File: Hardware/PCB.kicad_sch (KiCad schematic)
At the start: 9 parts, among them J1 Conn_01x04_Pin, U1 ME54BS01_V1.0, U2 MCP1700x-330xxTO

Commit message: Work on PCB
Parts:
- J1: footprint (none) -> Connector_PinHeader_2.54mm:PinHeader_1x04_P2.54mm_Vertical
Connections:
- net +3.3V: no longer S1.3
- net GND: no longer U1.1 (GND)
- net dividerPower1: now also U1.3 (P1.10)
- net dividerPower2: now also U1.4 (P1.11/AIN4)
- net reset: now also U1.24 (P0.01)
- no-connect marks 21 -> 23
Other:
- note added: "Was using battery connector footpring Connector_JST:JST_PH_S2B-PH-K_1x02_P2.00mm_Horizontal"
- moved on the sheet: BATT1, J1, Probe1, Probe2, R1, R2, S1, U1, U2

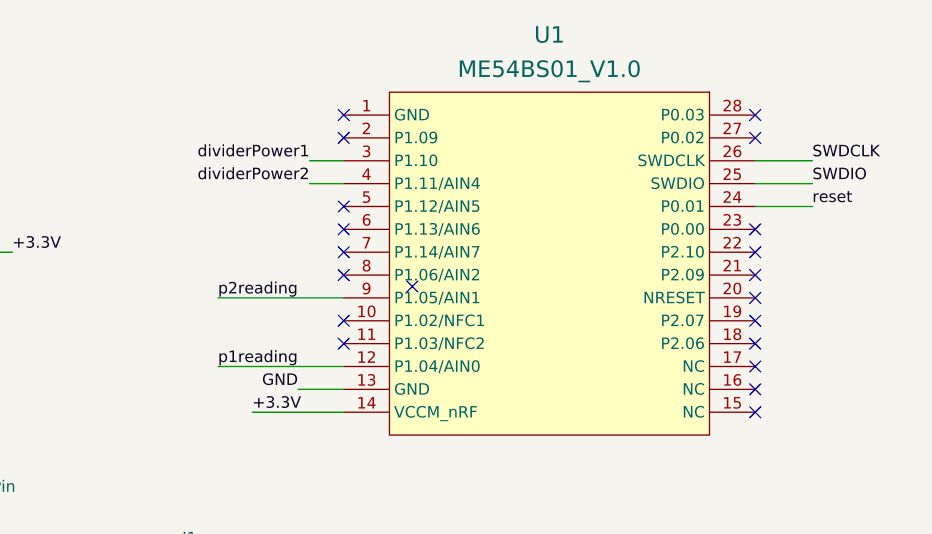
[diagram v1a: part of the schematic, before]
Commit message: Update PCB with new pin outs
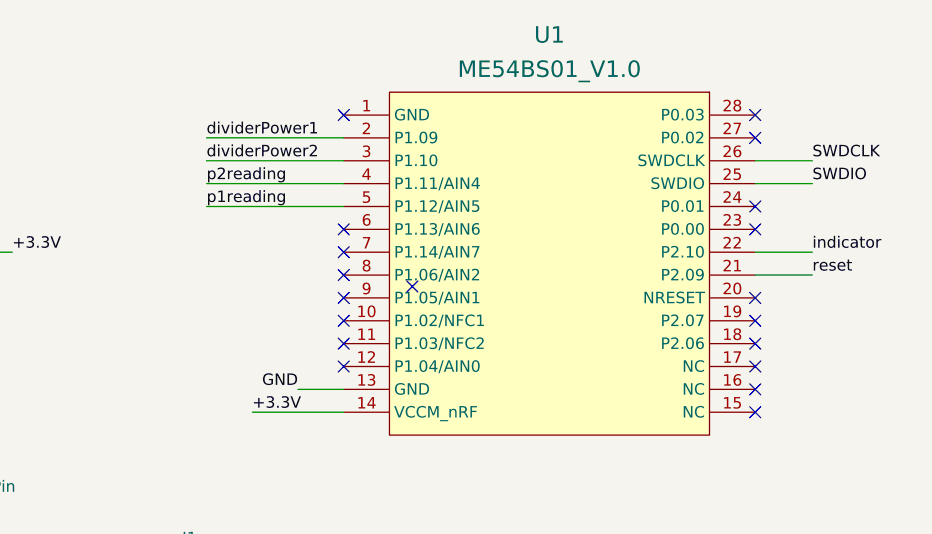
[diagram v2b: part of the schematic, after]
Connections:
- net dividerPower1: now also U1.2 (P1.09); no longer U1.3 (P1.10)
- net dividerPower2: now also U1.3 (P1.10); no longer U1.4 (P1.11/AIN4)
- net p1reading: now also U1.5 (P1.12/AIN5); no longer U1.12 (P1.04/AIN0)
- net p2reading: now also U1.4 (P1.11/AIN4); no longer U1.9 (P1.05/AIN1)
- net reset: now also U1.21 (P2.09); no longer U1.24 (P0.01)
- net indicator: now reaches U1.22 (P2.10)
- no-connect marks 23 -> 22
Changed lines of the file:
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@@
 	)
 	(no_connect
-		(at 154.94 38.1)
+		(at 200.66 38.1)
 	)
 	(no_connect
@@
 	)
 	(no_connect
+		(at 154.94 48.26)
+	)
+	(no_connect
+		(at 154.94 40.64)
+	)
+	(no_connect
 		(at 200.66 30.48)
 	)
@@
 	)
 	(no_connect
-		(at 200.66 43.18)
+		(at 200.66 60.96)
+	)
+	(no_connect
+		(at 33.02 45.72)
+	)
+	(no_connect
+		(at 200.66 50.8)
 	)
 	(no_connect
@@
 	)
 	(no_connect
-		(at 200.66 60.96)
-	)
-	(no_connect
-		(at 154.94 30.48)
-	)
-	(no_connect
-		(at 33.02 45.72)
-	)
-	(no_connect
-		(at 200.66 50.8)
-	)
-	(no_connect
-		(at 200.66 45.72)
-	)
-	(no_connect
 		(at 33.02 35.56)
 	)
 	(no_connect
-		(at 154.94 40.64)
+		(at 154.94 55.88)
 	)
 	(no_connect
@@
 	(wire
 		(pts
+			(xy 139.7 30.48) (xy 154.94 30.48)
+		)
+		(stroke
+			(width 0)
+			(type default)
+		)
+	)
+	(wire
+		(pts
 			(xy 102.87 76.2) (xy 106.68 76.2)
 		)
@@
 	(wire
 		(pts
-			(xy 151.13 35.56) (xy 154.94 35.56)
-		)
-		(stroke
-			(width 0)
-			(type default)
-		)
-	)
-	(wire
-		(pts
-			(xy 200.66 38.1) (xy 207.01 38.1)
-		)
-		(stroke
-			(width 0)
-			(type default)
-		)
-	)
-	(wire
-		(pts
 			(xy 142.24 85.09) (xy 148.59 85.09)
 		)
@@
 	(wire
 		(pts
-			(xy 154.94 55.88) (xy 140.97 55.88)
+			(xy 200.66 43.18) (xy 207.01 43.18)
 		)
 		(stroke
@@
 	(wire
 		(pts
-			(xy 154.94 48.26) (xy 140.97 48.26)
-		)
-		(stroke
-			(width 0)
-			(type default)
-		)
-	)
-	(wire
-		(pts
-			(xy 151.13 33.02) (xy 154.94 33.02)
+			(xy 139.7 35.56) (xy 154.94 35.56)
 		)
 		(stroke
@@
 	(wire
 		(pts
+			(xy 200.66 45.72) (xy 207.01 45.72)
+		)
+		(stroke
+			(width 0)
+			(type default)
+		)
+	)
+	(wire
+		(pts
 			(xy 58.42 45.72) (xy 60.96 45.72)
 		)
@@
 	(wire
 		(pts
+			(xy 139.7 38.1) (xy 154.94 38.1)
+		)
+		(stroke
+			(width 0)
+			(type default)
+		)
+	)
+	(wire
+		(pts
 			(xy 64.77 85.09) (xy 64.77 90.17)
 		)
@@
 			(width 0)
 			(type default)
+		)
+	)
+	(wire
+		(pts
+			(xy 139.7 33.02) (xy 154.94 33.02)
+		)
+		(stroke
+			(width 0)
+			(type default)
+		)
+	)
+	(label "p2reading"
+		(at 139.7 35.56 0)
+		(effects
+			(font
+				(size 1.27 1.27)
+			)
+			(justify left bottom)
 		)
 	)
@@
 		)
 	)
-	(label "p2reading"
-		(at 140.97 48.26 0)
+	(label "indicator"
+		(at 207.01 43.18 0)
 		(effects
 			(font
@@
 	)
 	(label "p1reading"
-		(at 140.97 55.88 0)
-		(effects
-			(font
-				(size 1.27 1.27)
-			)
-			(justify left bottom)
-		)
-	)
-	(label "dividerPower1"
-		(at 151.13 33.02 180)
-		(effects
-			(font
-				(size 1.27 1.27)
-			)
-			(justify right bottom)
+		(at 139.7 38.1 0)
+		(effects
+			(font
+				(size 1.27 1.27)
+			)
+			(justify left bottom)
+		)
+	)
+	(label "dividerPower2"
+		(at 139.7 33.02 0)
+		(effects
+			(font
+				(size 1.27 1.27)
+			)
+			(justify left bottom)
 		)
 	)
@@
 		)
 	)
-	(label "reset"
-		(at 207.01 38.1 0)
-		(effects
-			(font
-				(size 1.27 1.27)
-			)
-			(justify left bottom)
-		)
-	)
 	(label "dividerPower2"
 		(at 64.77 90.17 0)
@@
 		)
 	)
+	(label "reset"
+		(at 207.01 45.72 0)
+		(effects
+			(font
+				(size 1.27 1.27)
+			)
+			(justify left bottom)
+		)
+	)
 	(label "dividerPower1"
 		(at 36.83 90.17 0)
@@
 		)
 	)
-	(label "dividerPower2"
-		(at 151.13 35.56 180)
-		(effects
-			(font
-				(size 1.27 1.27)
-			)
-			(justify right bottom)
-		)
-	)
+	(label "dividerPower1"
+		(at 139.7 30.48 0)
+		(effects
+			(font
+				(size 1.27 1.27)
+			)
+			(justify left bottom)
+		)
+	)

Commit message: Update the PCB
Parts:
- added D1: LED, LED_SMD:LED_0805_2012Metric, symbol Device:LED
- added R4: R, Resistor_SMD:R_0805_2012Metric, symbol Device:R
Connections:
- net GND: now also D1.1 (K)
- net indicator: now also R4.2
- new net: D1.2 (A), R4.1
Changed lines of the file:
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@@
+	(wire
+		(pts
+			(xy 195.58 83.82) (xy 198.12 83.82)
+		)
+		(stroke
+			(width 0)
+			(type default)
+		)
+	)
 	(wire
 		(pts
@@
 		(pts
 			(xy 44.45 71.12) (xy 39.37 71.12)
+		)
+		(stroke
+			(width 0)
+			(type default)
+		)
+	)
+	(wire
+		(pts
+			(xy 186.69 83.82) (xy 187.96 83.82)
 		)
 		(stroke
@@
 		)
 	)
+	(label "GND"
+		(at 179.07 83.82 180)
+		(effects
+			(font
+				(size 1.27 1.27)
+			)
+			(justify right bottom)
+		)
+	)
 	(label "indicator"
 		(at 207.01 43.18 0)
@@
 	(label "p1reading"
 		(at 24.13 73.66 0)
+		(effects
+			(font
+				(size 1.27 1.27)
+			)
+			(justify left bottom)
+		)
+	)
+	(label "indicator"
+		(at 198.12 83.82 0)
 		(effects
 			(font
@@
 	)
 	(symbol
+		(lib_id "Device:LED")
+		(at 182.88 83.82 0)
+		(unit 1)
+		(exclude_from_sim no)
+		(in_bom yes)
+		(on_board yes)
+		(dnp no)
+		(fields_autoplaced yes)
+		(property "Reference" "D1"
+			(at 181.2925 77.47 0)
+			(effects
+				(font
+					(size 1.27 1.27)
+				)
+			)
+		)
+		(property "Value" "LED"
+			(at 181.2925 80.01 0)
+			(effects
+				(font
+					(size 1.27 1.27)
+				)
+			)
+		)
+		(property "Footprint" "LED_SMD:LED_0805_2012Metric"
+			(at 182.88 83.82 0)
+			(effects
+				(font
+					(size 1.27 1.27)
+				)
+				(hide yes)
+			)
+		)
+		(property "Datasheet" "~"
+			(at 182.88 83.82 0)
+			(effects
+				(font
+					(size 1.27 1.27)
+				)
+				(hide yes)
+			)
+		)
+		(property "Description" "Light emitting diode"
+			(at 182.88 83.82 0)
+			(effects
+				(font
+					(size 1.27 1.27)
+				)
+				(hide yes)
+			)
+		)
+		(property "Sim.Pins" "1=K 2=A"
+			(at 182.88 83.82 0)
+			(effects
+				(font
+					(size 1.27 1.27)
+				)
+				(hide yes)
+			)
+		)
+		(pin "1"
+		)
+		(pin "2"
+		)
+		(instances
+			(project ""
+				(path "/9240e15d-484a-49b3-8f80-37d1a010783e"
+					(reference "D1")
+					(unit 1)
+				)
+			)
+		)
+	)
+	(symbol
 		(lib_id "ME54BS01-1Y15TI:ME54BS01_V1.0")
 		(at 160.02 63.5 0)
@@
 					(unit 1)
 				)
+			)
+		)
+	)
+	(symbol
+		(lib_id "Device:R")
+		(at 191.77 83.82 90)
+		(unit 1)
+		(exclude_from_sim no)
+		(in_bom yes)
+		(on_board yes)
+		(dnp no)
+		(fields_autoplaced yes)
+		(property "Reference" "R4"
+			(at 191.77 77.47 90)
+			(effects
+				(font
+					(size 1.27 1.27)
+				)
+			)
+		)
+		(property "Value" "R"
+			(at 191.77 80.01 90)
+			(effects
+				(font
+					(size 1.27 1.27)
+				)
+			)
+		)
+		(property "Footprint" "Resistor_SMD:R_0805_2012Metric"
+			(at 191.77 85.598 90)
+			(effects
+				(font
+					(size 1.27 1.27)
+				)
+				(hide yes)
+			)
+		)
+		(property "Datasheet" "~"
+			(at 191.77 83.82 0)
+			(effects
+				(font
+					(size 1.27 1.27)
+				)
+				(hide yes)
+			)
+		)
+		(property "Description" "Resistor"
+			(at 191.77 83.82 0)
+			(effects
+				(font
+					(size 1.27 1.27)
+				)
+				(hide yes)
+			)
+		)
+		(pin "1"
+		)
+		(pin "2"
+		)
+		(instances
+			(project ""
+				(path "/9240e15d-484a-49b3-8f80-37d1a010783e"
+					(reference "R4")
+					(unit 1)
+				)

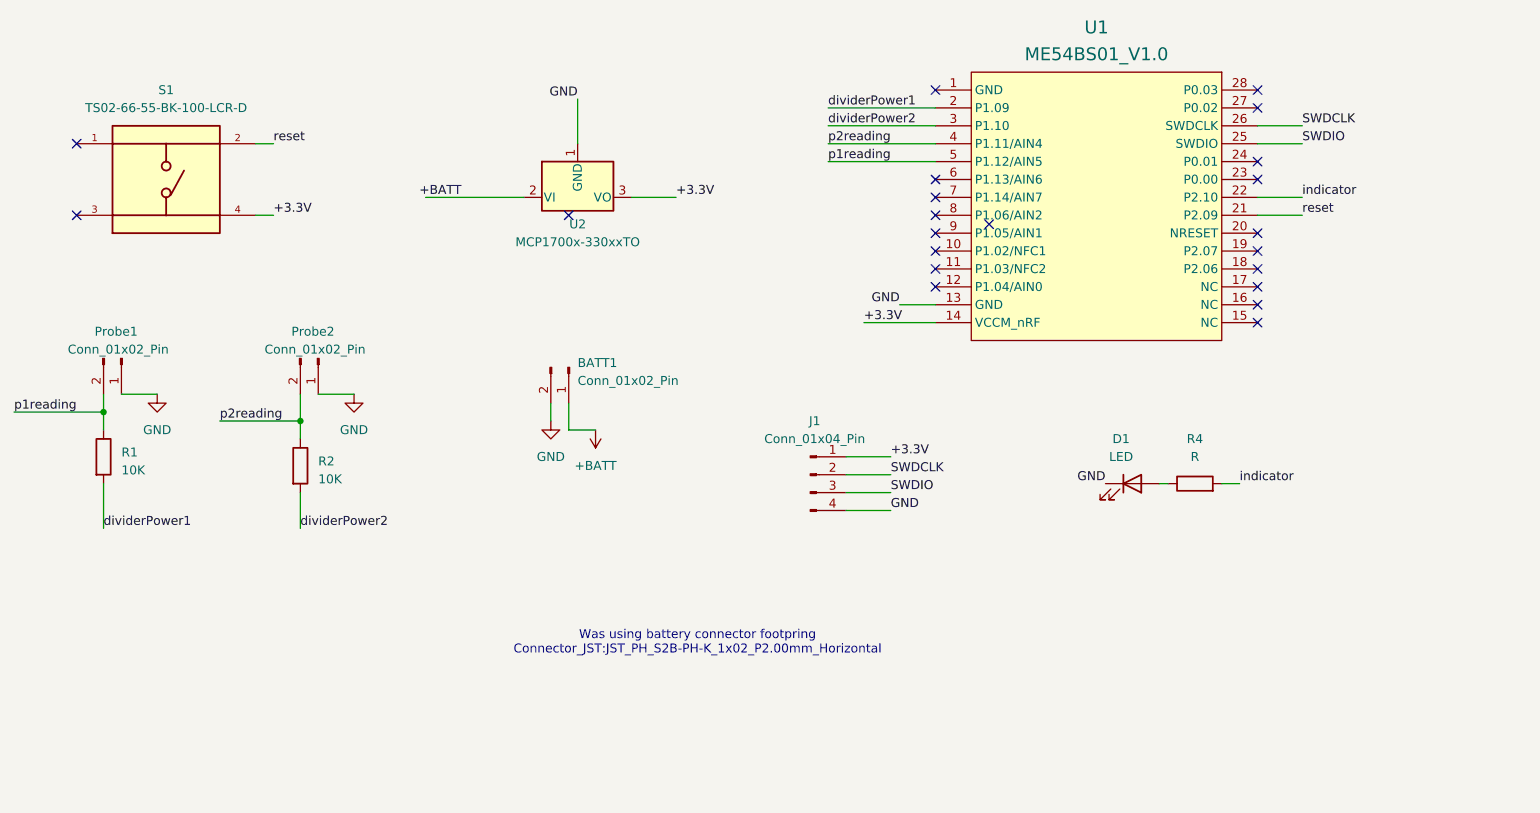
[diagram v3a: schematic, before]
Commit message: WIP Reworking schematic with Reddit feedback
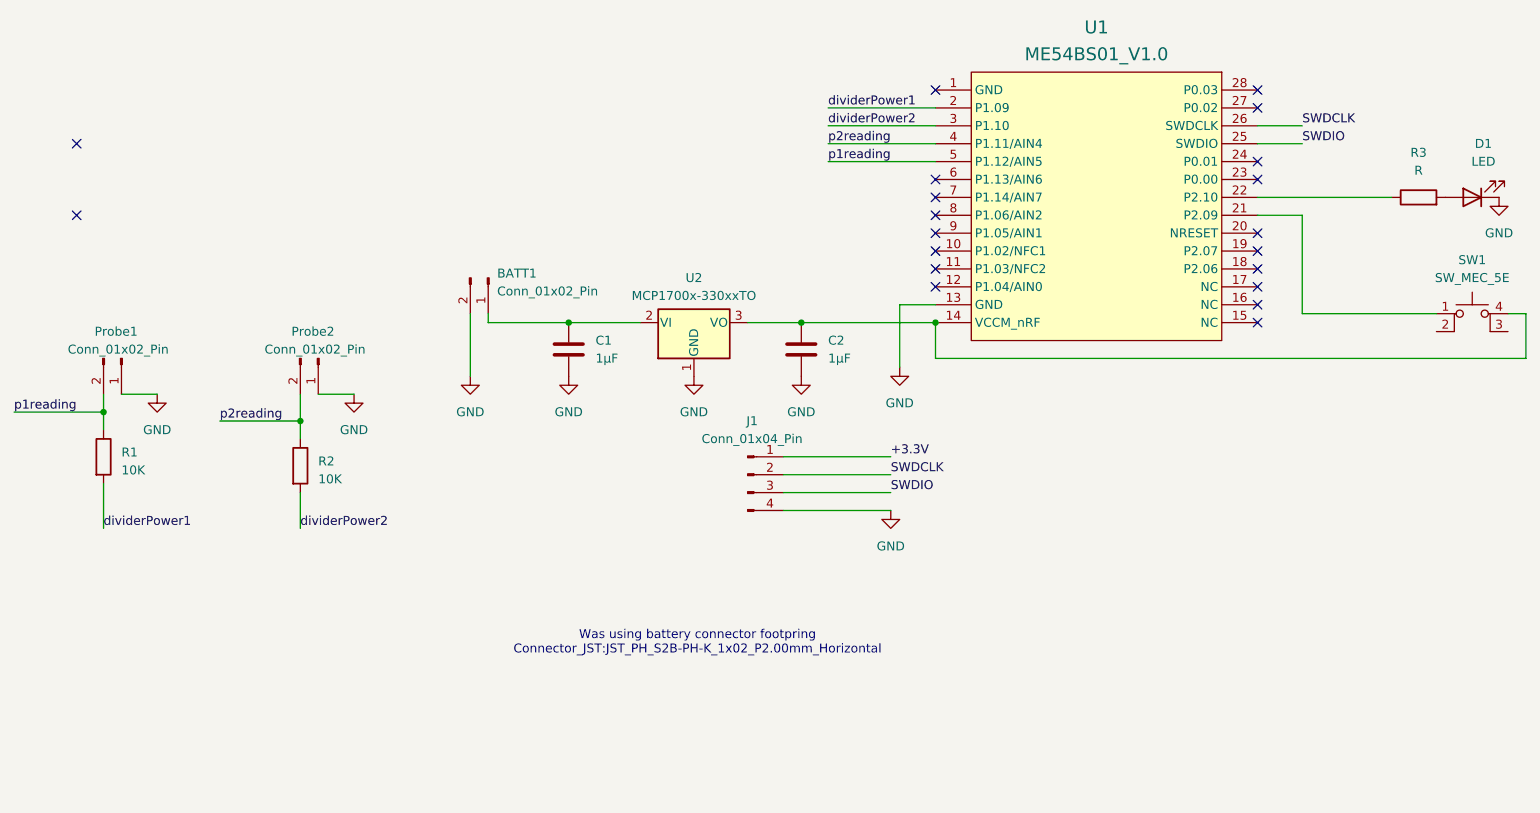
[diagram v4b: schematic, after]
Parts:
- removed S1: TS02-66-55-BK-100-LCR-D, TS02-66-55-BK-100-LCR-D:SW_TS02-66-55-BK-100-LCR-D, symbol TS02:TS02-66-55-BK-100-LCR-D
- added C1, C2: 1µF, symbol Device:C
- added SW1: SW_MEC_5E, TS02-66-55-BK-100-LCR-D:SW_TS02-66-55-BK-100-LCR-D, symbol Switch:SW_MEC_5E
- renumbered R4 to R3
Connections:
- net +3.3V: no longer U1.14 (VCCM_nRF), U2.3 (VO)
- net GND: now also C1.2, C2.2
- net at D1.2 (A): now also R3.2; no longer R3.1
- net +BATT: no longer names the net of BATT1.1 (Pin_1), U2.2 (VI)
- net +BATT: now also C1.1
- net indicator: no longer names the net of U1.22 (P2.10)
- net indicator: now also R3.1; no longer R3.2
- net reset: no longer names the net of U1.21 (P2.09)
- net reset: now also SW1.1
- new net: C2.1, SW1.4 (A), U1.14 (VCCM_nRF), U2.3 (VO)
- no-connect marks 22 -> 20
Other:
- moved on the sheet: BATT1, D1, J1, R3, U2

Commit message: Cleaned up schematic to be all in one. Trying to get updated layout for PCB
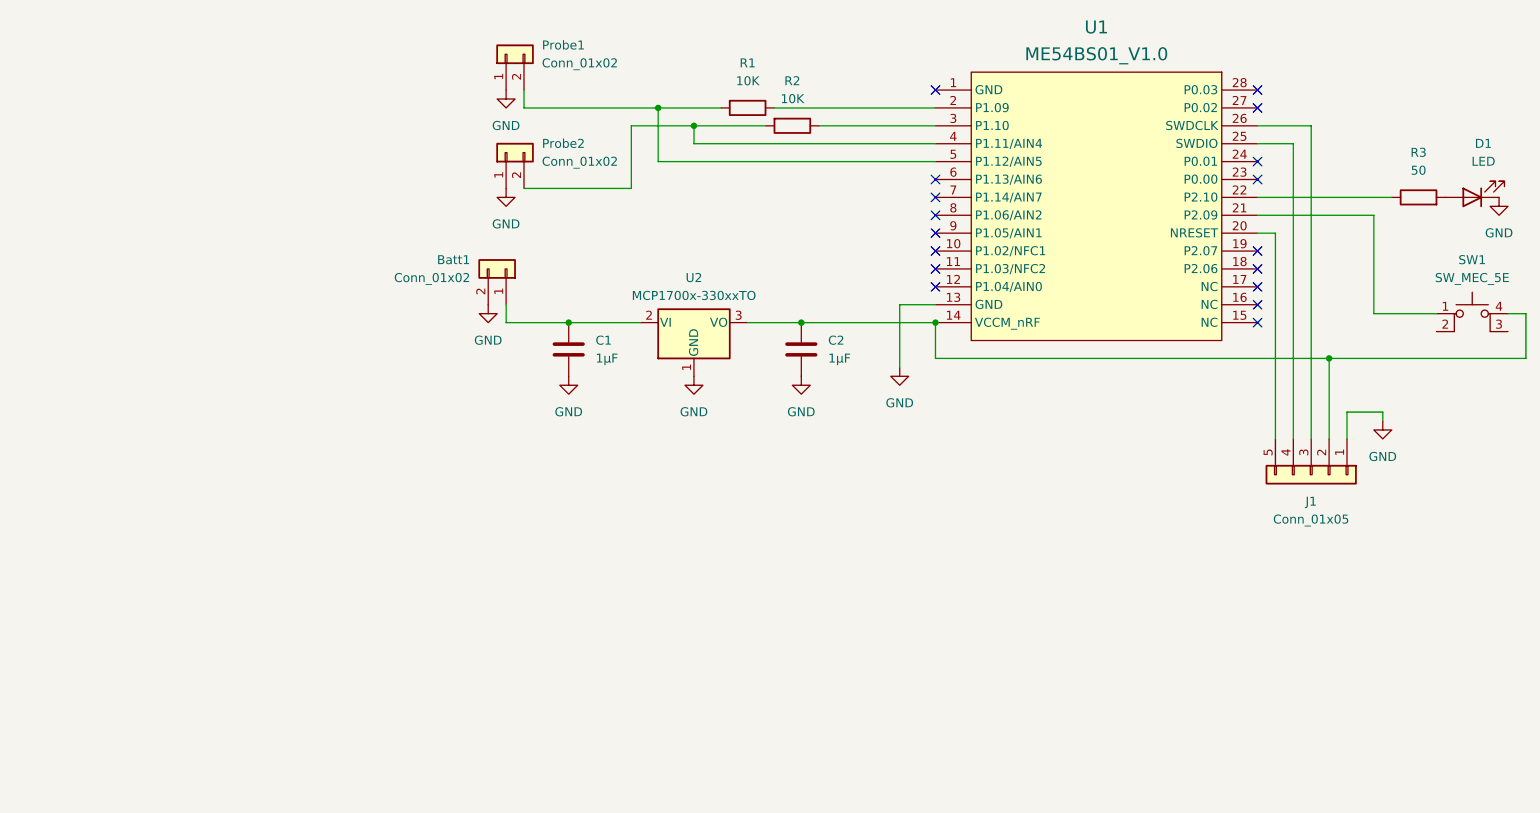
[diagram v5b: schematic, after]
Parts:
- removed BATT1, Probe1, Probe2: Conn_01x02_Pin, Connector_JST:JST_PH_S2B-PH-K_1x02_P2.00mm_Horizontal, symbol Connector:Conn_01x02_Pin
- removed J1: Conn_01x04_Pin, Connector_PinHeader_2.54mm:PinHeader_1x04_P2.54mm_Vertical, symbol Connector:Conn_01x04_Pin
- added Batt1, Probe1, Probe2: Conn_01x02, Connector_JST:JST_PH_S2B-PH-K_1x02_P2.00mm_Horizontal, symbol Connector_Generic:Conn_01x02
- added J1: Conn_01x05, Connector_PinHeader_2.54mm:PinHeader_1x05_P2.54mm_Vertical, symbol Connector_Generic:Conn_01x05
- C1, C2: footprint (none) -> Capacitor_SMD:C_0805_2012Metric
- R3: value R -> 50
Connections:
- net GND: now also Batt1.2 (Pin_2), J1.1 (Pin_1), Probe1.1 (Pin_1), Probe2.1 (Pin_1)
- net at C1.1, U2.2 (VI): now also Batt1.1 (Pin_1)
- net at C2.1, SW1.4 (A), U1.14 (VCCM_nRF)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: now also J1.2 (Pin_2)
- net at U1.20 (NRESET): now also J1.5 (Pin_5)
- net SWDCLK: no longer names the net of U1.26 (SWDCLK)
- net SWDCLK: now also J1.3 (Pin_3)
- net SWDIO: no longer names the net of U1.25 (SWDIO)
- net SWDIO: now also J1.4 (Pin_4)
- net dividerPower1: no longer names the net of R1.2
- net dividerPower1: now also U1.5 (P1.12/AIN5), Probe1.2 (Pin_2); no longer U1.2 (P1.09)
- net dividerPower2: no longer names the net of R2.2
- net dividerPower2: now also U1.4 (P1.11/AIN4), Probe2.2 (Pin_2); no longer U1.3 (P1.10)
- net p1reading: no longer names the net of R1.1
- net p1reading: now also U1.2 (P1.09); no longer U1.5 (P1.12/AIN5)
- net p2reading: no longer names the net of R2.1
- net p2reading: now also U1.3 (P1.10); no longer U1.4 (P1.11/AIN4)
- no-connect marks 20 -> 17
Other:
- note removed: "Was using battery connector footpring Connector_JST:JST_PH_S2B-PH-K_1x02_P2.00mm_Horizontal"
- moved on the sheet: R1, R2
